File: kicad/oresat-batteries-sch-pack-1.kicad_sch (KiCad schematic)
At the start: 84 parts, among them Q10 SI7625DN-T1-GE3, Q12 SI7625DN-T1-GE3, Q13 SI7625DN-T1-GE3, Q14 NTR4101, Q15 NTR4101, Q16 SI7625DN-T1-GE3, Q17 SI7625DN-T1-GE3, Q18 SI7625DN-T1-GE3, Q19 SI7625DN-T1-GE3, Q22 Si7336ADP, Q6 PM45VEN, Q7 PM45VEN, Q8 PM45VEN, Q9 PM45VEN, U10 LTC4412, U11 LTC4412, U12 MAX17205G, U8 S-8209AAA-T8T1U, U9 S-8209AAA-T8T1U

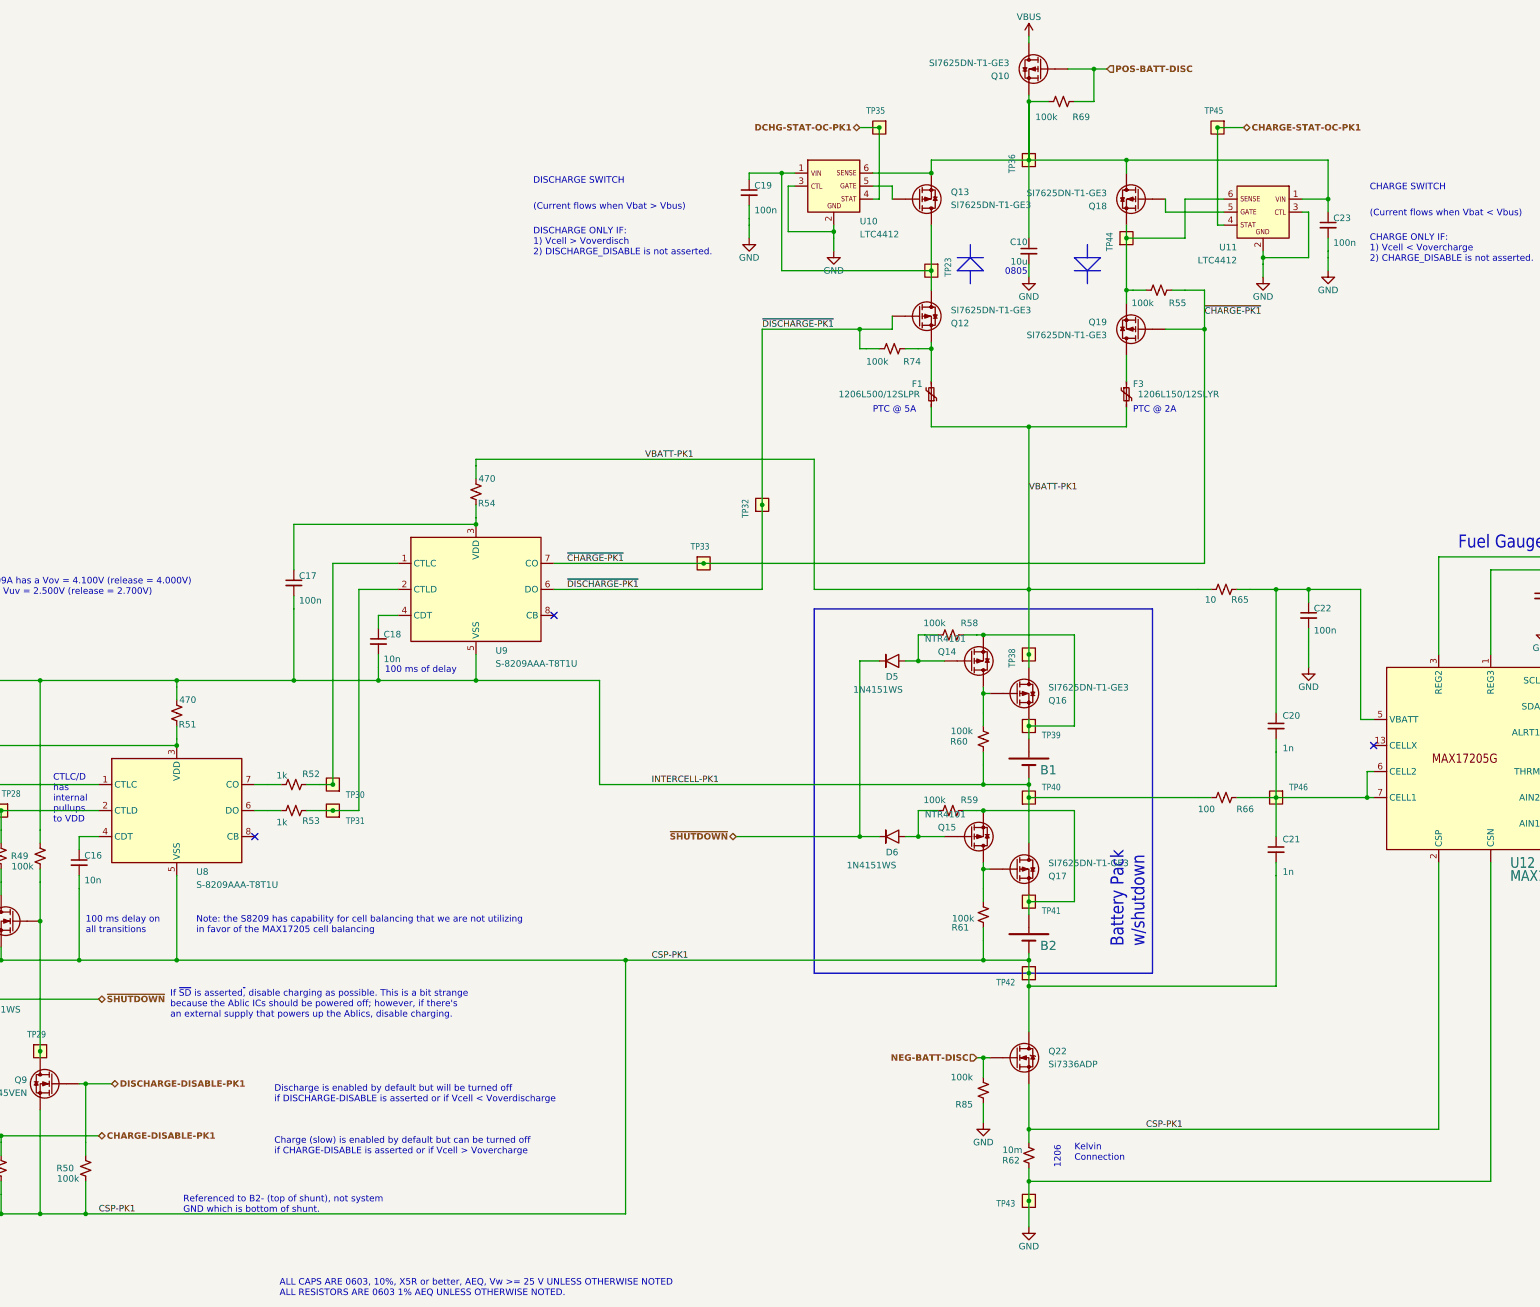
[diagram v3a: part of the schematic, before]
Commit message: Progress on v4
Figure out to bypass negative battery cutoff with 10k to make sure that nSHUTDOWN always works. Lots of moving around (it's tight), finally got pack 1 done. Working on the Pack 2.
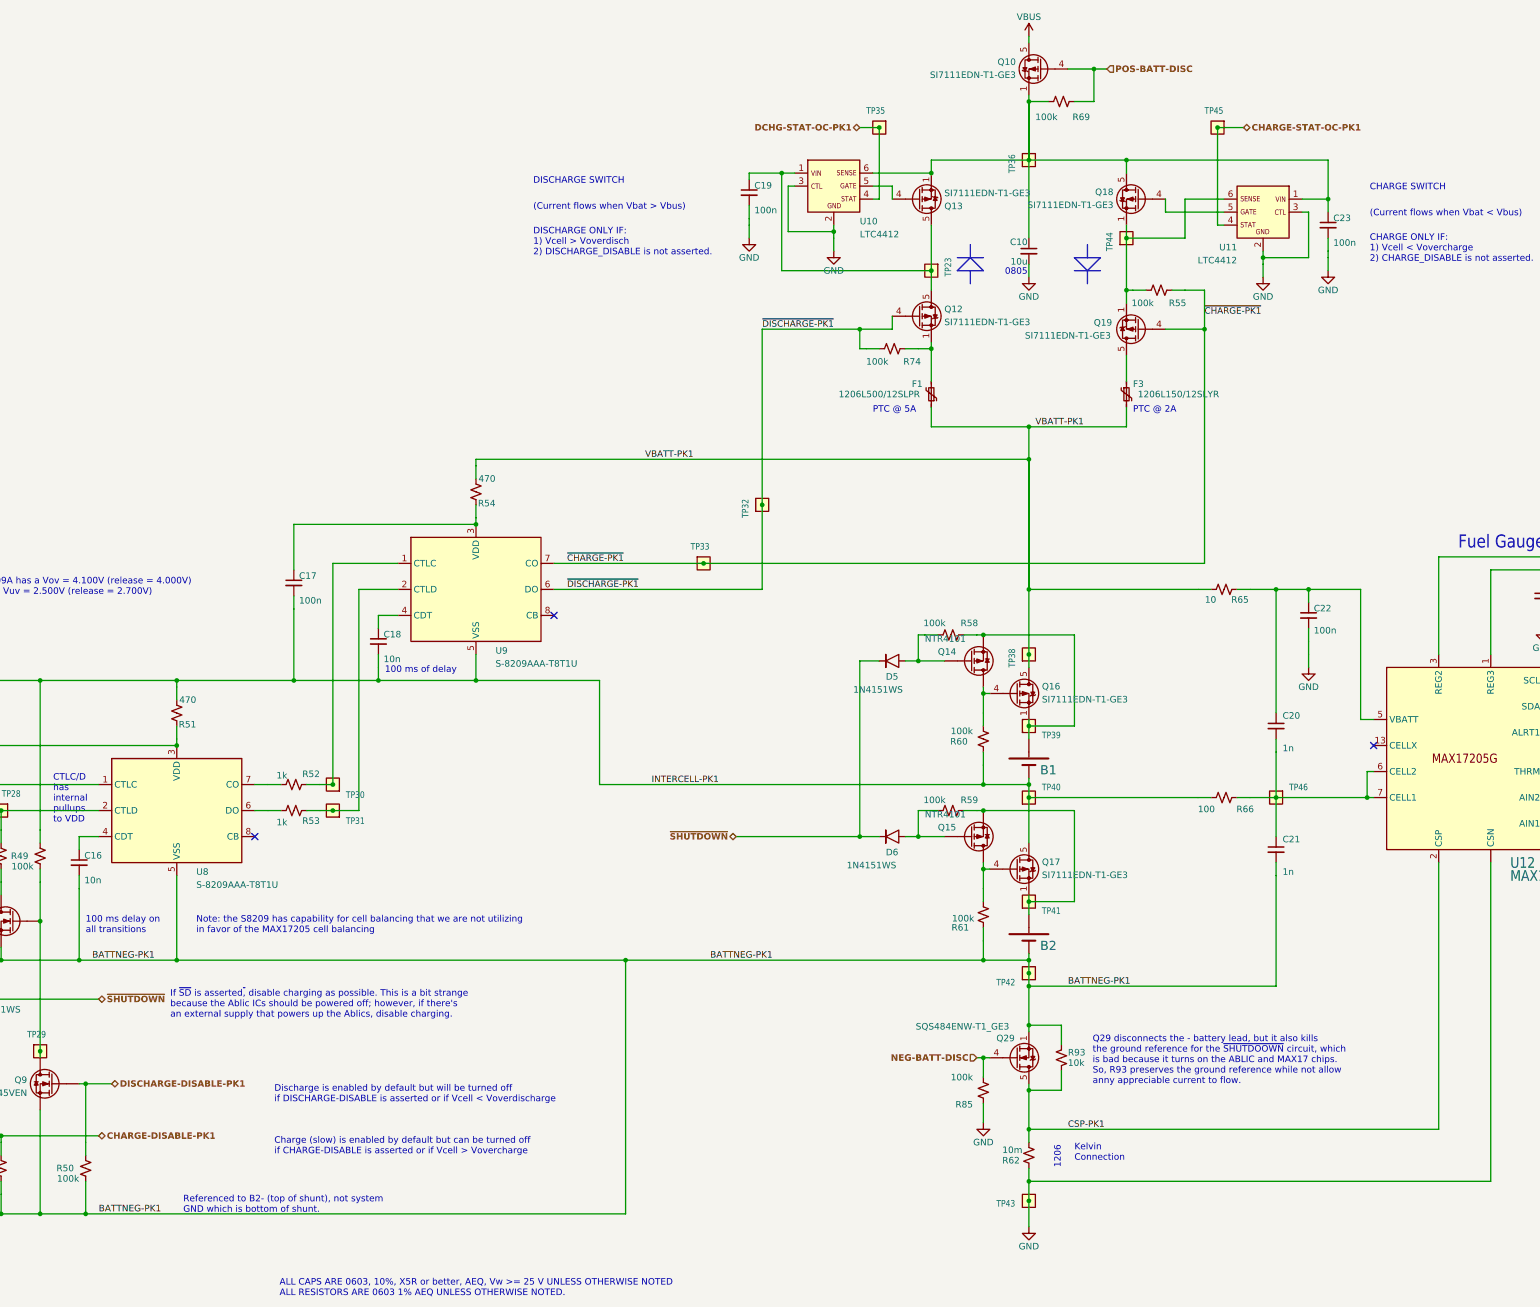
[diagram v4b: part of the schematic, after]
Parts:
- removed Q22: Si7336ADP, Package_SO:PowerPAK_SO-8_Single, symbol Transistor_FET:Si7336ADP
- added Q29: SQS484ENW-T1_GE3, Package_SO:Vishay_PowerPAK_1212-8_Single, symbol Transistor_FET:SiS454DN
- added R93: 10k, oresat-batteries:.0603-C-NOSILK, symbol Device:R_Small_US
- Q10, Q12, Q13, Q16, Q17, Q18, Q19: value SI7625DN-T1-GE3 -> SI7111EDN-T1-GE3; footprint oresat-batteries:POWERPAK-1212-8 -> Package_SO:Vishay_PowerPAK_1212-8_Single; symbol oresat-batteries-eagle-import:Q-VISHAY-MOSFET-PCH-POWERPAK-1212-8 -> Transistor_FET:SiS443DN
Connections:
- net CSP-PK1: now also Q29.5 (D), R93.1; no longer B2.2 (NEG), C15.2, C16.2, C21.2, Q6.2 (S), Q7.2 (S), Q8.2 (S), Q9.2 (S), R47.1, R50.1, R61.2, TP42.1, U8.5 (VSS)
- net NEG-BATT-DISC: now also Q29.4 (G)
- net at C10.1, C23.1, Q10.1 (S)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: now also Q10.2 (S), Q10.3 (S), Q13.2 (S), Q13.3 (S)
- net at B2.1 (POS), Q15.2 (S), Q17.1 (S)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: now also Q17.2 (S), Q17.3 (S)
- net at B1.1 (POS), Q14.2 (S), Q16.1 (S)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: now also Q16.2 (S), Q16.3 (S)
- net at Q18.1 (S), Q19.1 (S), R55.2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: now also Q18.2 (S), Q18.3 (S), Q19.2 (S), Q19.3 (S)
- net at F1.2, Q12.1 (S), R74.1: now also Q12.2 (S), Q12.3 (S)
- new net BATTNEG-PK1: B2.2 (NEG), C15.2, C16.2, C21.2, Q29.1 (S), Q29.2 (S), Q29.3 (S), Q6.2 (S), Q7.2 (S), Q8.2 (S), Q9.2 (S), R47.1, R50.1, R61.2, R93.2, TP42.1, U8.5 (VSS)
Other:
- note added: "Q29 disconnects the - battery lead, but it also kills the ground reference for the ~{SHUTDOOWN} circuit, which is bad because it turns on the ABLIC and MAX17 chips. So, R93 preserves the ground reference while not allow anny appreciable current to flow."
- note removed: "Battery Pack w/shutdown"

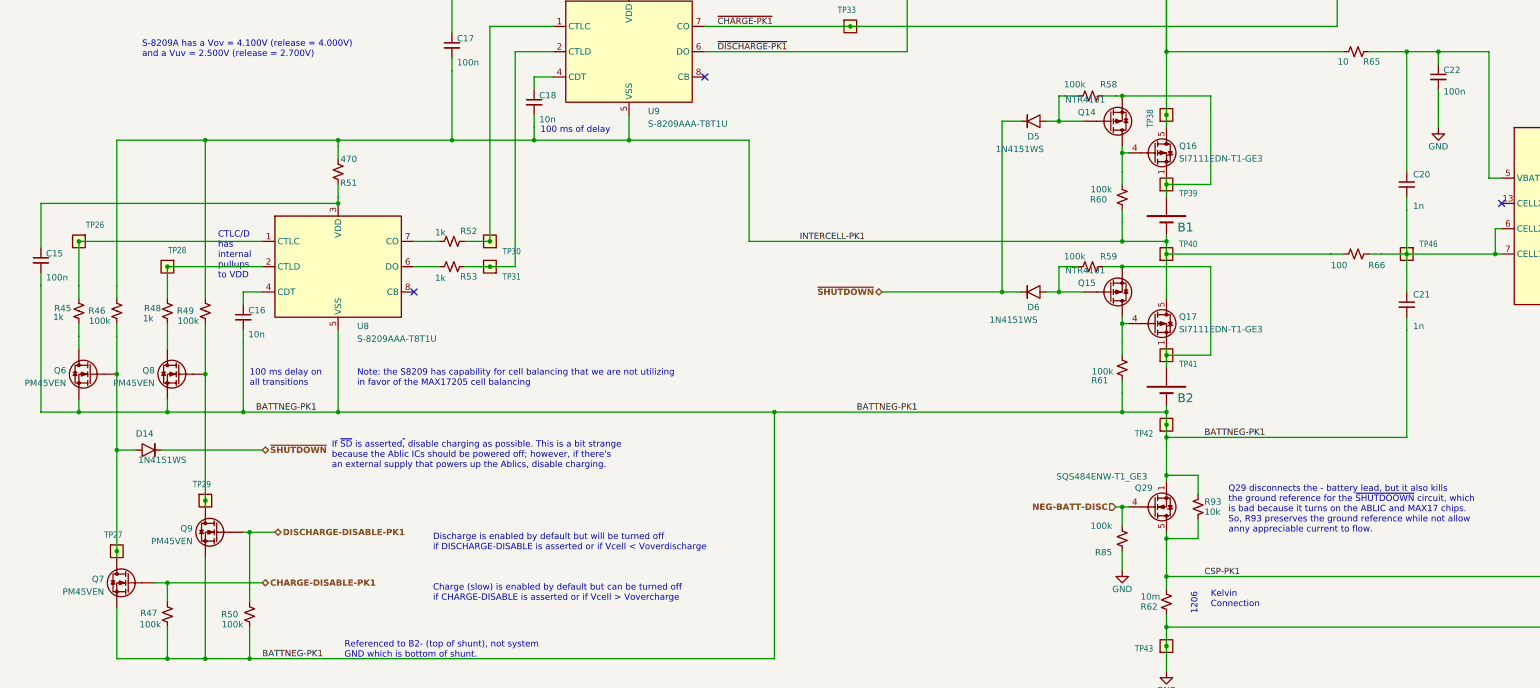
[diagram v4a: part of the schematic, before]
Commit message: Progress on battery card v4
Moved in -batt cutoffs, which caused a lot of pain and suffering. Started updating BOM, and fixed all transistor packages. Updated resistor packages, too. Still needs a lot of cleanup, but probably 80% done now.
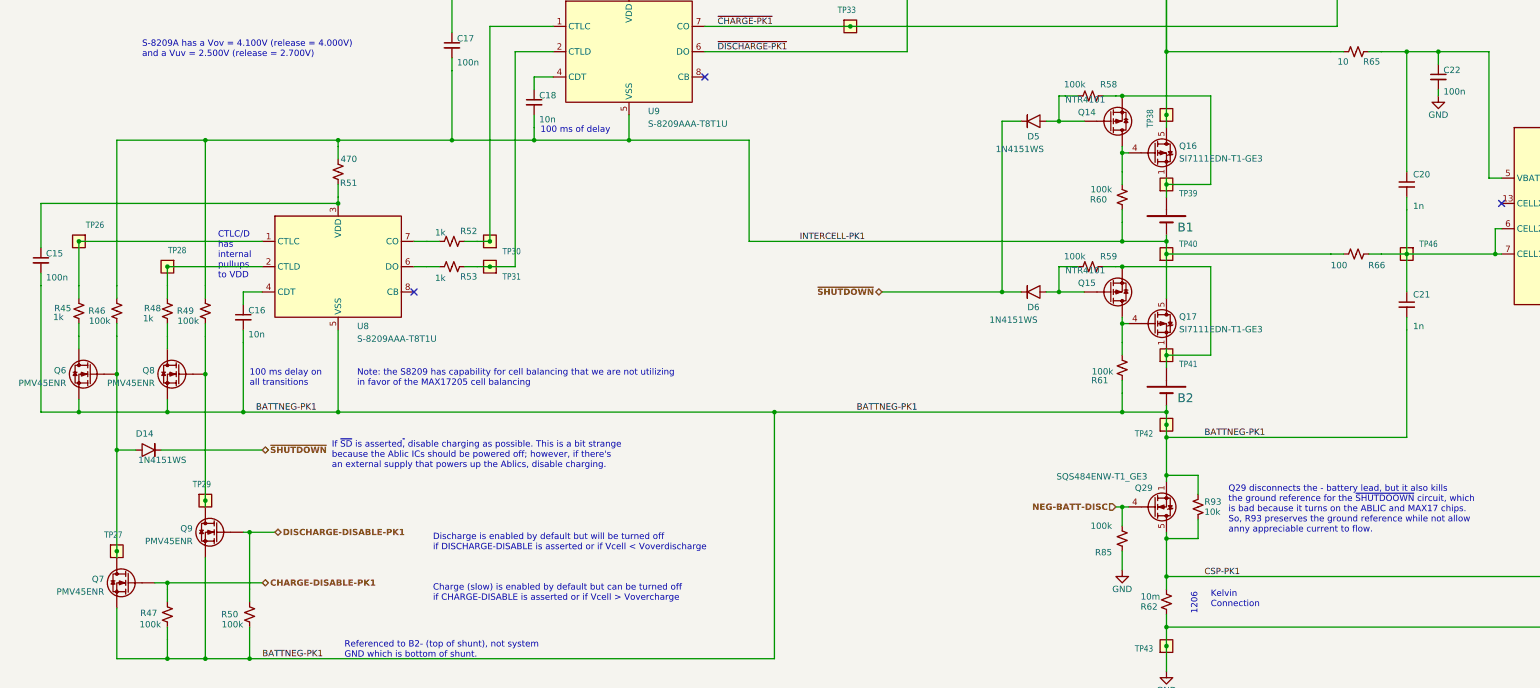
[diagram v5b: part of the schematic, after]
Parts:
- C10: footprint oresat-batteries:.0805-B-NOSILK -> oresat-passives:0805-C-NOSILK
- C15, C16, C17, C18, C19, C20, C21, C22, C23, C24, C25: footprint oresat-passives:c_0603-SMALL -> oresat-passives:0603-C-NOSILK
- Q10, Q12, Q13, Q16, Q17, Q18, Q19: DIS Digi-Key -> DigiKey
- Q14, Q15: footprint oresat-batteries:SOT23-3 -> Package_TO_SOT_SMD:SOT-23; DIS Digi-Key -> DigiKey
- Q29: DIS (none) -> DigiKey
- Q6, Q7, Q8, Q9: value PM45VEN -> PMV45ENR; footprint oresat-batteries:SOT23-3 -> Package_TO_SOT_SMD:SOT-23; DIS Digi-Key -> DigiKey
- R45, R46, R47, R48, R49, R50, R51, R52, R53, R54, R55, R58, R59, R60, R61, R69, R73, R74, R85, R93: footprint oresat-batteries:.0603-C-NOSILK -> oresat-passives:0603-C-NOSILK
- R62: footprint oresat-batteries:1206-C -> oresat-passives:1206-C
- R65, R66: footprint oresat-batteries:.0603-C-NOSILK -> oresat-passives:0603-C-NOSILK; DIS Digi-Key -> DigiKey
- R71: footprint oresat-batteries:.0603-C-NOSILK -> oresat-passives:0603-C-NOSILK; DISTRIBUTOR Digi-key -> (none)
